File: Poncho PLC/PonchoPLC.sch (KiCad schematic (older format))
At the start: 5 parts, among them J1 I2C, J2 RS-232

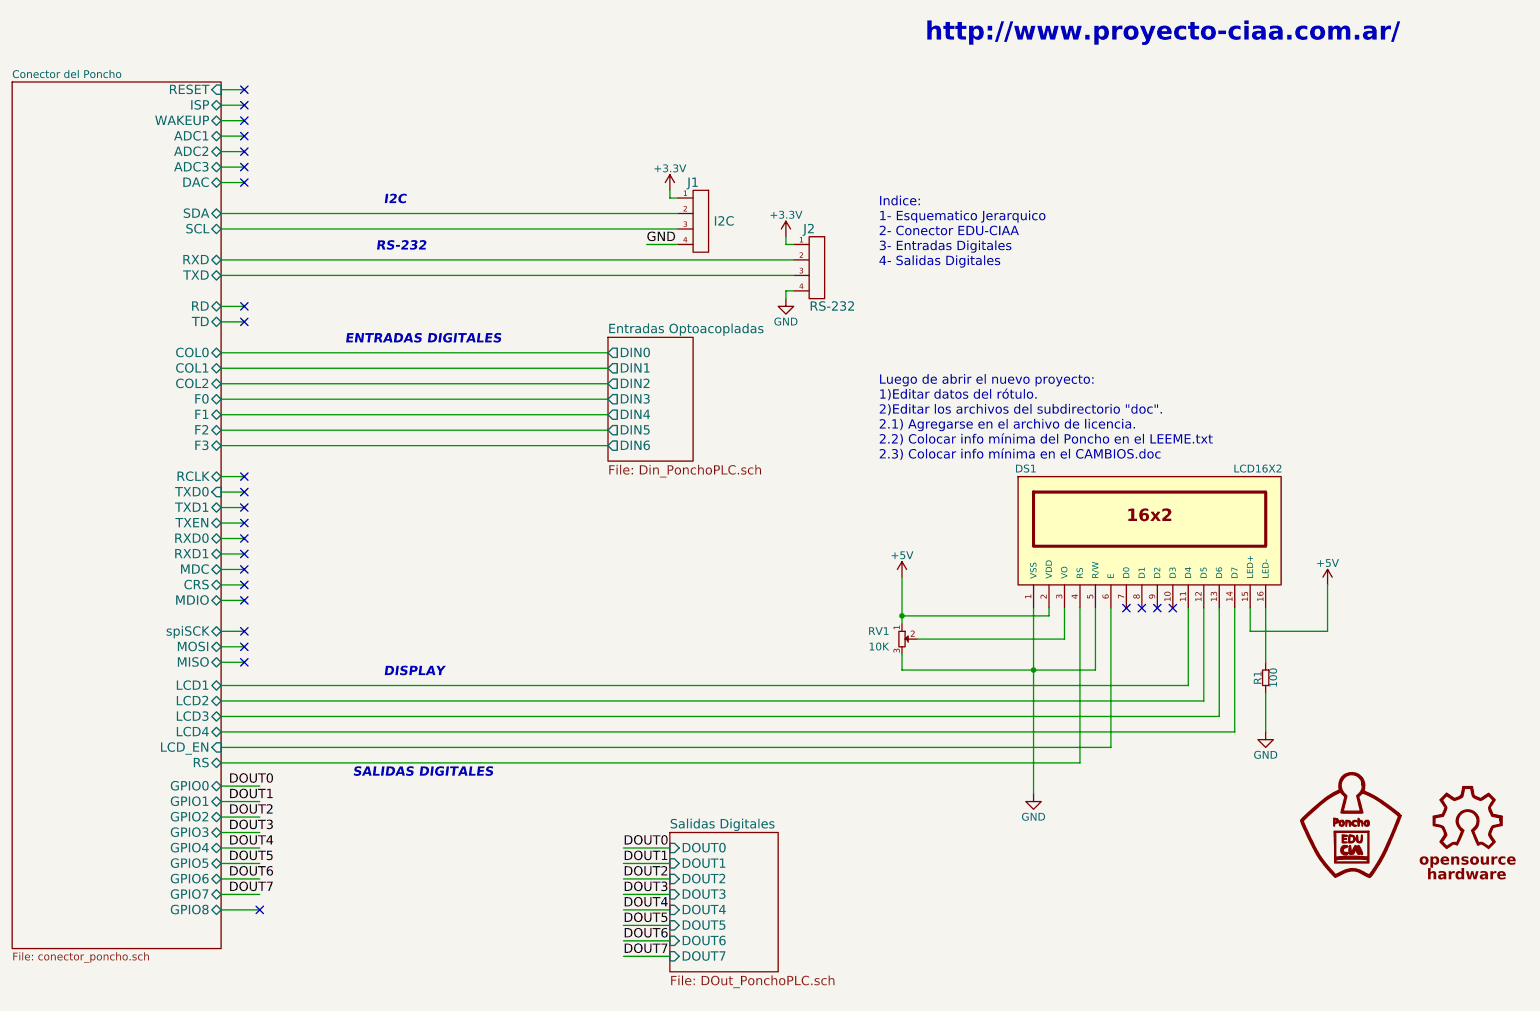
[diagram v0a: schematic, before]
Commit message: Detalles de la hoja principal de Poncho-PLC.
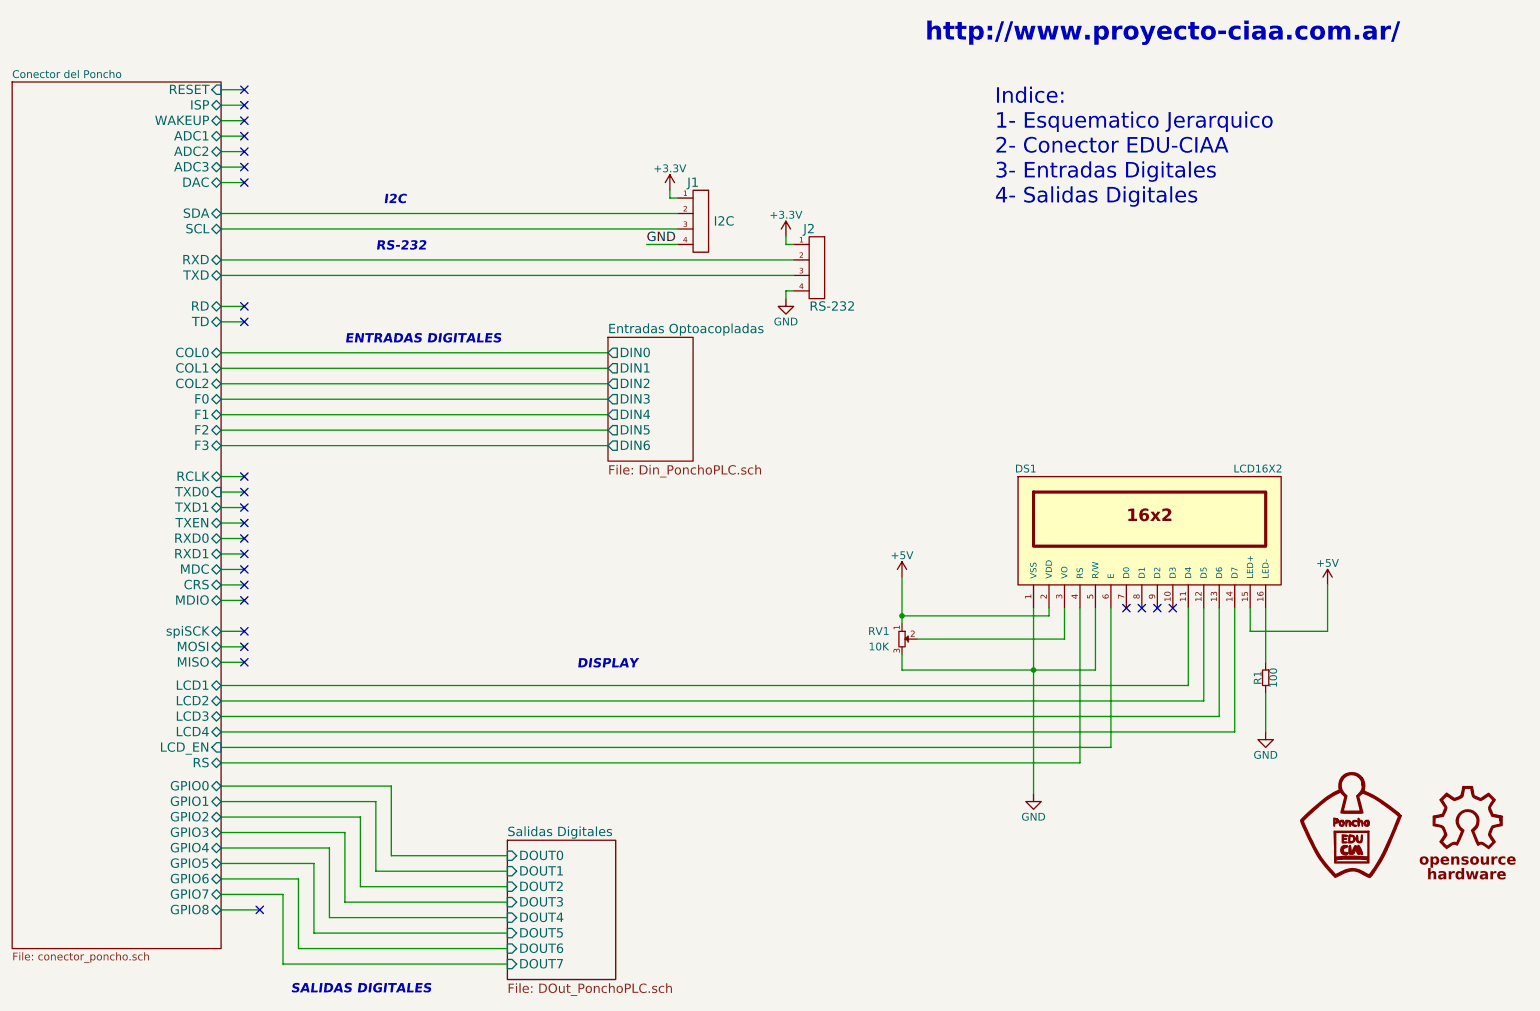
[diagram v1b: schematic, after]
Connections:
- net labels removed: DOUT0, DOUT1, DOUT2, DOUT3, DOUT4, DOUT5, DOUT6, DOUT7
- wire segments 82 -> 90
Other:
- note removed: "Luego de abrir el nuevo proyecto:\n1)Editar datos del rótulo.\n2)Editar los archivos del subdirectorio "doc".\n2.1) Agregarse en el archivo de licencia.\n2.2) Colocar info mínima del Poncho en el LEEME.txt\n2.3) Colocar info mínima en el CAMBIOS.doc"
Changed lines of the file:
@@
 Text Notes 3550 2900 0    60   Italic 12
 ENTRADAS DIGITALES
-Text Notes 3800 5050 0    60   Italic 12
+Text Notes 5050 5000 0    60   Italic 12
 DISPLAY
-Text Notes 3600 5700 0    60   Italic 12
+Text Notes 3200 7100 0    60   Italic 12
 SALIDAS DIGITALES
 Text Notes 7300 950  0    118  ~ 24
 http://www.proyecto-ciaa.com.ar/
-Text Notes 7000 3650 0    60   ~ 0
-Luego de abrir el nuevo proyecto:\n1)Editar datos del rótulo.\n2)Editar los archivos del subdirectorio "doc".\n2.1) Agregarse en el archivo de licencia.\n2.2) Colocar info mínima del Poncho en el LEEME.txt\n2.3) Colocar info mínima en el CAMBIOS.doc
-Text Notes 7000 2400 0    60   ~ 0
+Text Notes 7750 2000 0    100  ~ 0
 Indice:\n1- Esquematico Jerarquico\n2- Conector EDU-CIAA\n3- Entradas Digitales\n4- Salidas Digitales
 $Sheet
@@
 NoConn ~ 2900 2650
 $Sheet
-S 5650 6050 700  900
+S 4600 6100 700  900
 U 56AC5E66
 F0 "Salidas Digitales" 60
 F1 "DOut_PonchoPLC.sch" 60
-F2 "DOUT1" I L 5650 6250 60
-F3 "DOUT3" I L 5650 6450 60
-F4 "DOUT0" I L 5650 6150 60
-F5 "DOUT2" I L 5650 6350 60
-F6 "DOUT4" I L 5650 6550 60
-F7 "DOUT5" I L 5650 6650 60
-F8 "DOUT6" I L 5650 6750 60
-F9 "DOUT7" I L 5650 6850 60
+F2 "DOUT1" I L 4600 6300 60
+F3 "DOUT3" I L 4600 6500 60
+F4 "DOUT0" I L 4600 6200 60
+F5 "DOUT2" I L 4600 6400 60
+F6 "DOUT4" I L 4600 6600 60
+F7 "DOUT5" I L 4600 6700 60
+F8 "DOUT6" I L 4600 6800 60
+F9 "DOUT7" I L 4600 6900 60
 $EndSheet
 Wire Wire Line
@@
 	2900 2750 2750 2750
 Wire Wire Line
-	3000 5750 2750 5750
-Wire Wire Line
-	3000 5850 2750 5850
-Wire Wire Line
-	3000 5950 2750 5950
-Wire Wire Line
-	3000 6050 2750 6050
-Wire Wire Line
-	3000 6150 2750 6150
-Wire Wire Line
-	3000 6250 2750 6250
-Wire Wire Line
-	3000 6350 2750 6350
-Wire Wire Line
-	3000 6450 2750 6450
-Text Label 2800 5750 0    60   ~ 0
-DOUT0
-Text Label 2800 5850 0    60   ~ 0
-DOUT1
-Text Label 2800 5950 0    60   ~ 0
-DOUT2
-Text Label 2800 6050 0    60   ~ 0
-DOUT3
-Text Label 2800 6150 0    60   ~ 0
-DOUT4
-Text Label 2800 6250 0    60   ~ 0
-DOUT5
-Text Label 2800 6350 0    60   ~ 0
-DOUT6
-Text Label 2800 6450 0    60   ~ 0
-DOUT7
-Wire Wire Line
-	5350 6150 5650 6150
-Wire Wire Line
-	5350 6250 5650 6250
-Wire Wire Line
-	5350 6350 5650 6350
-Wire Wire Line
-	5350 6450 5650 6450
-Wire Wire Line
-	5350 6550 5650 6550
-Wire Wire Line
-	5350 6650 5650 6650
-Wire Wire Line
-	5350 6750 5650 6750
-Wire Wire Line
-	5350 6850 5650 6850
-Text Label 5350 6150 0    60   ~ 0
-DOUT0
-Text Label 5350 6250 0    60   ~ 0
-DOUT1
-Text Label 5350 6350 0    60   ~ 0
-DOUT2
-Text Label 5350 6450 0    60   ~ 0
-DOUT3
-Text Label 5350 6550 0    60   ~ 0
-DOUT4
-Text Label 5350 6650 0    60   ~ 0
-DOUT5
-Text Label 5350 6750 0    60   ~ 0
-DOUT6
-Text Label 5350 6850 0    60   ~ 0
-DOUT7
+	2750 5750 3850 5750
+Wire Wire Line
+	2750 5850 3750 5850
+Wire Wire Line
+	2750 5950 3650 5950
+Wire Wire Line
+	2750 6050 3550 6050
+Wire Wire Line
+	2750 6150 3450 6150
+Wire Wire Line
+	2750 6250 3350 6250
+Wire Wire Line
+	2750 6350 3250 6350
+Wire Wire Line
+	2750 6450 3150 6450
+Wire Wire Line
+	3850 6200 4600 6200
+Wire Wire Line
+	3750 6300 4600 6300
+Wire Wire Line
+	3650 6400 4600 6400
+Wire Wire Line
+	3550 6500 4600 6500
+Wire Wire Line
+	3450 6600 4600 6600
+Wire Wire Line
+	3350 6700 4600 6700
+Wire Wire Line
+	3250 6800 4600 6800
+Wire Wire Line
+	3150 6900 4600 6900
 Wire Wire Line
 	3000 6550 2750 6550
@@
 $EndComp
 Wire Wire Line
-	7150 4700 7150 4400
+	7150 4400 7150 4700
 Wire Wire Line
 	7150 4650 8100 4650
@@
 NoConn ~ 8800 4600
 NoConn ~ 8900 4600
+Wire Wire Line
+	3850 5750 3850 6200
+Wire Wire Line
+	3750 5850 3750 6300
+Wire Wire Line
+	3650 5950 3650 6400
+Wire Wire Line
+	3550 6050 3550 6500
+Wire Wire Line
+	3450 6150 3450 6600
+Wire Wire Line
+	3350 6250 3350 6700
+Wire Wire Line
+	3250 6350 3250 6800
+Wire Wire Line
+	3150 6450 3150 6900
 $EndSCHEMATC

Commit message: Cambio SCH
Se modificaron algunas etiquetas para beneficiar el routeo del pcb en la
conexión Rele-Bornera.
Se actualizaron las referencias de las huellas de la librería anterior a
la actual, para lograr compatibilidad en el netlist y poder cargarlo al
pcb.
Se actualizaron los filtros de búsqueda de huellas en algunos
componentes de la librería de sch.
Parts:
- DS1: footprint EESTN5:LCD_16x2 -> Poncho-PLC:LCD_16x2
- J1, J2: footprint EESTN5:HEADER-4H -> Poncho-PLC:HEADER-4H
- R1: footprint EESTN5:R_1206 -> Poncho-PLC:R_1206
- RV1: footprint EESTN5:TRIMER_V -> Poncho-PLC:TRIMER_V
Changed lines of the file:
@@
 F 0 "J1" H 5800 2350 60  0000 C CNN
 F 1 "I2C" H 6000 2100 60  0000 C CNN
-F 2 "EESTN5:HEADER-4H" H 5800 2100 60  0001 C CNN
+F 2 "Poncho-PLC:HEADER-4H" H 5800 2100 60  0001 C CNN
 F 3 "" H 5800 2100 60  0000 C CNN
 F 4 "Esqueleto EDU-CIAA" H 5800 2100 60  0001 C CNN "Title"
@@
 F 0 "J2" H 6550 2650 60  0000 C CNN
 F 1 "RS-232" H 6700 2150 60  0000 C CNN
-F 2 "EESTN5:HEADER-4H" H 6550 2400 60  0001 C CNN
+F 2 "Poncho-PLC:HEADER-4H" H 6550 2400 60  0001 C CNN
 F 3 "" H 6550 2400 60  0000 C CNN
 F 4 "Esqueleto EDU-CIAA" H 6550 2400 60  0001 C CNN "Title"
@@
 F 0 "DS1" H 7950 4500 50  0000 C CNN
 F 1 "LCD16X2" H 9450 4500 50  0000 C CNN
-F 2 "EESTN5:LCD_16x2" H 8750 4050 50  0001 C CIN
+F 2 "Poncho-PLC:LCD_16x2" H 8750 4050 50  0001 C CIN
 F 3 "" H 8750 4100 50  0000 C CNN
 F 4 "Esqueleto EDU-CIAA" H 8750 4100 60  0001 C CNN "Title"
@@
 F 0 "RV1" V 7100 4650 50  0000 C CNN
 F 1 "10K" V 7200 4650 50  0000 C CNN
-F 2 "EESTN5:TRIMER_V" H 7150 4800 60  0001 C CNN
+F 2 "Poncho-PLC:TRIMER_V" H 7150 4800 60  0001 C CNN
 F 3 "" H 7150 4800 60  0000 C CNN
 F 4 "Esqueleto EDU-CIAA" H 7150 4800 60  0001 C CNN "Title"
@@
 F 0 "R1" V 9450 5050 50  0000 C CNN
 F 1 "100" V 9550 5050 50  0000 C CNN
-F 2 "EESTN5:R_1206" H 9500 5050 60  0001 C CNN
+F 2 "Poncho-PLC:R_1206" H 9500 5050 60  0001 C CNN
 F 3 "" H 9500 5050 60  0000 C CNN
 F 4 "Esqueleto EDU-CIAA" H 10100 4950 60  0001 C CNN "Title"

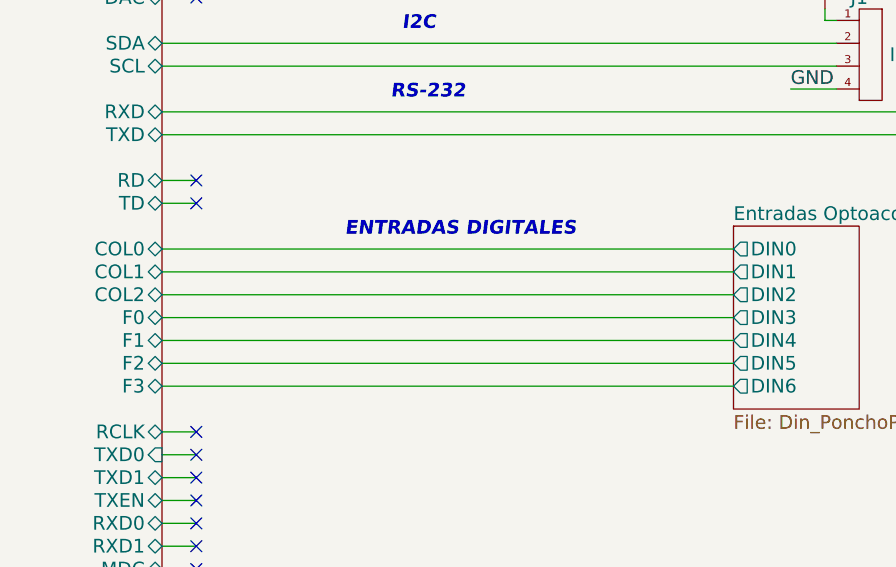
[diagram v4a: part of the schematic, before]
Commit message: Avance posicionamiento
Posicione las borneras de las entradas digitales.
Arregle el footprint de las borneras para que tengan un pitch de 100mils
Cambie a bottom layer algunos componentes para acercarme a un tamaño de
placa de 150X100mm
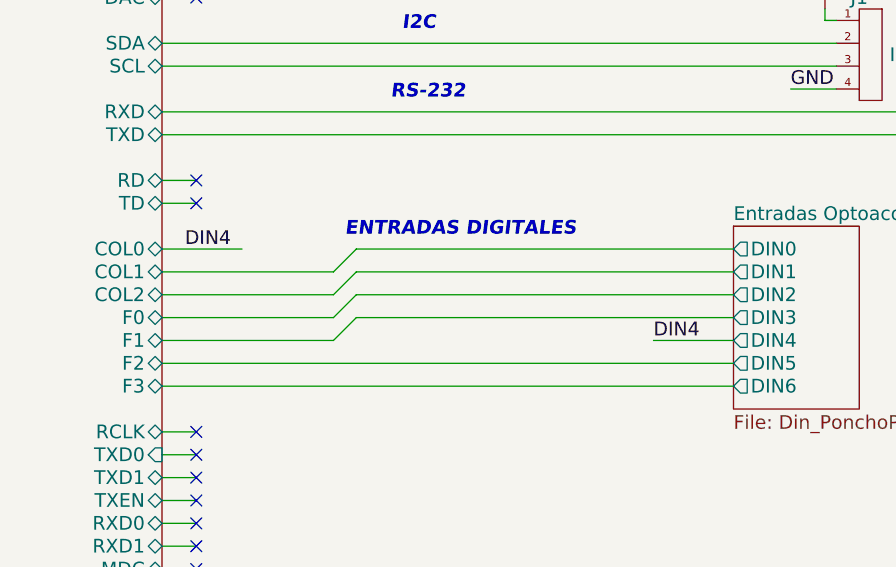
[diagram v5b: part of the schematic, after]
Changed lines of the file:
@@
 	5250 3450 2750 3450
-Wire Wire Line
-	2750 3350 5250 3350
-Wire Wire Line
-	5250 3250 2750 3250
-Wire Wire Line
-	2750 3150 5250 3150
-Wire Wire Line
-	5250 3050 2750 3050
-Wire Wire Line
-	2750 2950 5250 2950
 Wire Wire Line
 	2750 2450 6450 2450
@@
 Wire Wire Line
 	3150 6450 3150 6900
+Wire Wire Line
+	4900 3350 5250 3350
+Text Label 2850 2950 0    60   ~ 0
+DIN4
+Text Label 4900 3350 0    60   ~ 0
+DIN4
+Wire Wire Line
+	2750 3050 3500 3050
+Wire Wire Line
+	3500 3050 3600 2950
+Wire Wire Line
+	3600 2950 5250 2950
+Wire Wire Line
+	2750 3250 3500 3250
+Wire Wire Line
+	2750 3350 3500 3350
+Wire Wire Line
+	2750 3150 3500 3150
+Wire Wire Line
+	3500 3150 3600 3050
+Wire Wire Line
+	3600 3050 5250 3050
+Wire Wire Line
+	3500 3250 3600 3150
+Wire Wire Line
+	3600 3150 5250 3150
+Wire Wire Line
+	3500 3350 3600 3250
+Wire Wire Line
+	3600 3250 5250 3250
+Wire Wire Line
+	2750 2950 3100 2950
 $EndSCHEMATC

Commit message: Avances varios
Se avanzo en el routeo de la placa, solo quedan 7 conexiones.
Se incluyo el logo del proyecto CIAA.
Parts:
- J1: footprint Poncho-PLC:HEADER-4H -> EESTN5:JST-4V
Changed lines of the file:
@@
 F 0 "J1" H 5800 2350 60  0000 C CNN
 F 1 "I2C" H 6000 2100 60  0000 C CNN
-F 2 "Poncho-PLC:HEADER-4H" H 5800 2100 60  0001 C CNN
+F 2 "EESTN5:JST-4V" H 5800 2100 60  0001 C CNN
 F 3 "" H 5800 2100 60  0000 C CNN
 F 4 "Esqueleto EDU-CIAA" H 5800 2100 60  0001 C CNN "Title"

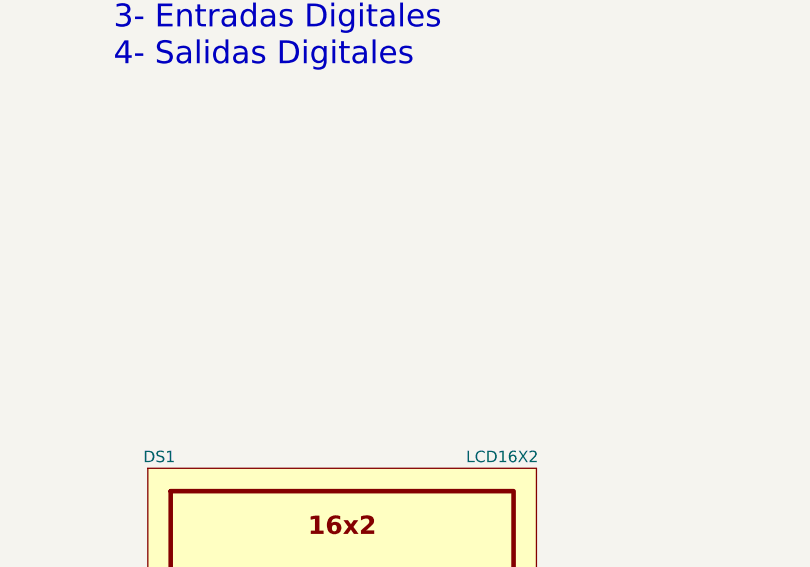
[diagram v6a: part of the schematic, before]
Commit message: Ajustes para fabricación
Se modifico la serigrafia de varios footprints para fabricación.
Se agregó el logo de ponchos en serigrafia.
Se modifico el contorno de la placa para que se puedan visualizar los
leds de la EDU-CIAA.
Se agregaron 4 Agujeros de sujeción para fijar la placa a la EDU-CIAA.
TO DO: Diseñar Piezas para imprimir en 3D.
Se cambio de lugar el logo de la escuela y el texto de proyecto CIAA
para mejor visualización.
TO DO:
Ajustar las referencias a librerias para portabilidad.
Actualizar la libreria del proyecto para que contenga todos los
footprints utilizados.
Generar BOM.
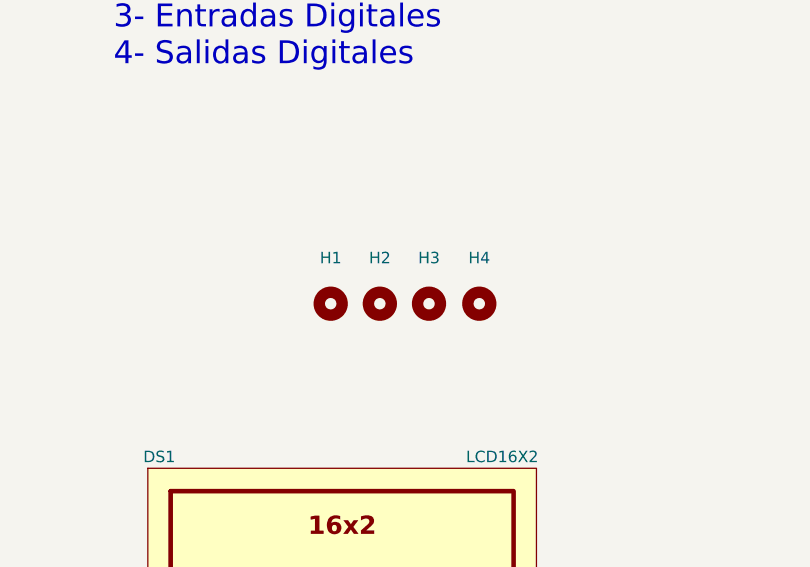
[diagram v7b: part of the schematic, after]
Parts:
- added H1, H2, H3, H4: Mounting_Hole, Poncho-PLC:Separador_M3_5mm, symbol Mounting_Hole
- J1: footprint EESTN5:JST-4V -> EESTN5:pin_strip_4
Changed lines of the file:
@@
 EESchema Schematic File Version 2
 LIBS:PonchoPLC
+LIBS:EESTN5
 LIBS:PonchoPLC-cache
 EELAYER 25 0
@@
 F 0 "J1" H 5800 2350 60  0000 C CNN
 F 1 "I2C" H 6000 2100 60  0000 C CNN
-F 2 "EESTN5:JST-4V" H 5800 2100 60  0001 C CNN
+F 2 "EESTN5:pin_strip_4" H 5800 2100 60  0001 C CNN
 F 3 "" H 5800 2100 60  0000 C CNN
 F 4 "Esqueleto EDU-CIAA" H 5800 2100 60  0001 C CNN "Title"
@@
 Wire Wire Line
 	2750 2950 3100 2950
+$Comp
+L Mounting_Hole H1
+U 1 1 592B9E9D
+P 8700 3030
+F 0 "H1" H 8700 3230 50  0000 C CNN
+F 1 "Mounting_Hole" H 8700 3155 50  0001 C CNN
+F 2 "Poncho-PLC:Separador_M3_5mm" H 8700 3030 60  0001 C CNN
+F 3 "" H 8700 3030 60  0001 C CNN
+	1    8700 3030
+	1    0    0    -1
+$EndComp
+$Comp
+L Mounting_Hole H2
+U 1 1 592BD1A6
+P 8915 3030
+F 0 "H2" H 8915 3230 50  0000 C CNN
+F 1 "Mounting_Hole" H 8915 3155 50  0001 C CNN
+F 2 "Poncho-PLC:Separador_M3_5mm" H 8915 3030 60  0001 C CNN
+F 3 "" H 8915 3030 60  0001 C CNN
+	1    8915 3030
+	1    0    0    -1
+$EndComp
+$Comp
+L Mounting_Hole H3
+U 1 1 592BD309
+P 9130 3030
+F 0 "H3" H 9130 3230 50  0000 C CNN
+F 1 "Mounting_Hole" H 9130 3155 50  0001 C CNN
+F 2 "Poncho-PLC:Separador_M3_5mm" H 9130 3030 60  0001 C CNN
+F 3 "" H 9130 3030 60  0001 C CNN
+	1    9130 3030
+	1    0    0    -1
+$EndComp
+$Comp
+L Mounting_Hole H4
+U 1 1 592BD30F
+P 9350 3030
+F 0 "H4" H 9350 3230 50  0000 C CNN
+F 1 "Mounting_Hole" H 9350 3155 50  0001 C CNN
+F 2 "Poncho-PLC:Separador_M3_5mm" H 9350 3030 60  0001 C CNN
+F 3 "" H 9350 3030 60  0001 C CNN
+	1    9350 3030
+	1    0    0    -1
+$EndComp
 $EndSCHEMATC
